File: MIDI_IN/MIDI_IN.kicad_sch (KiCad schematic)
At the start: 25 parts

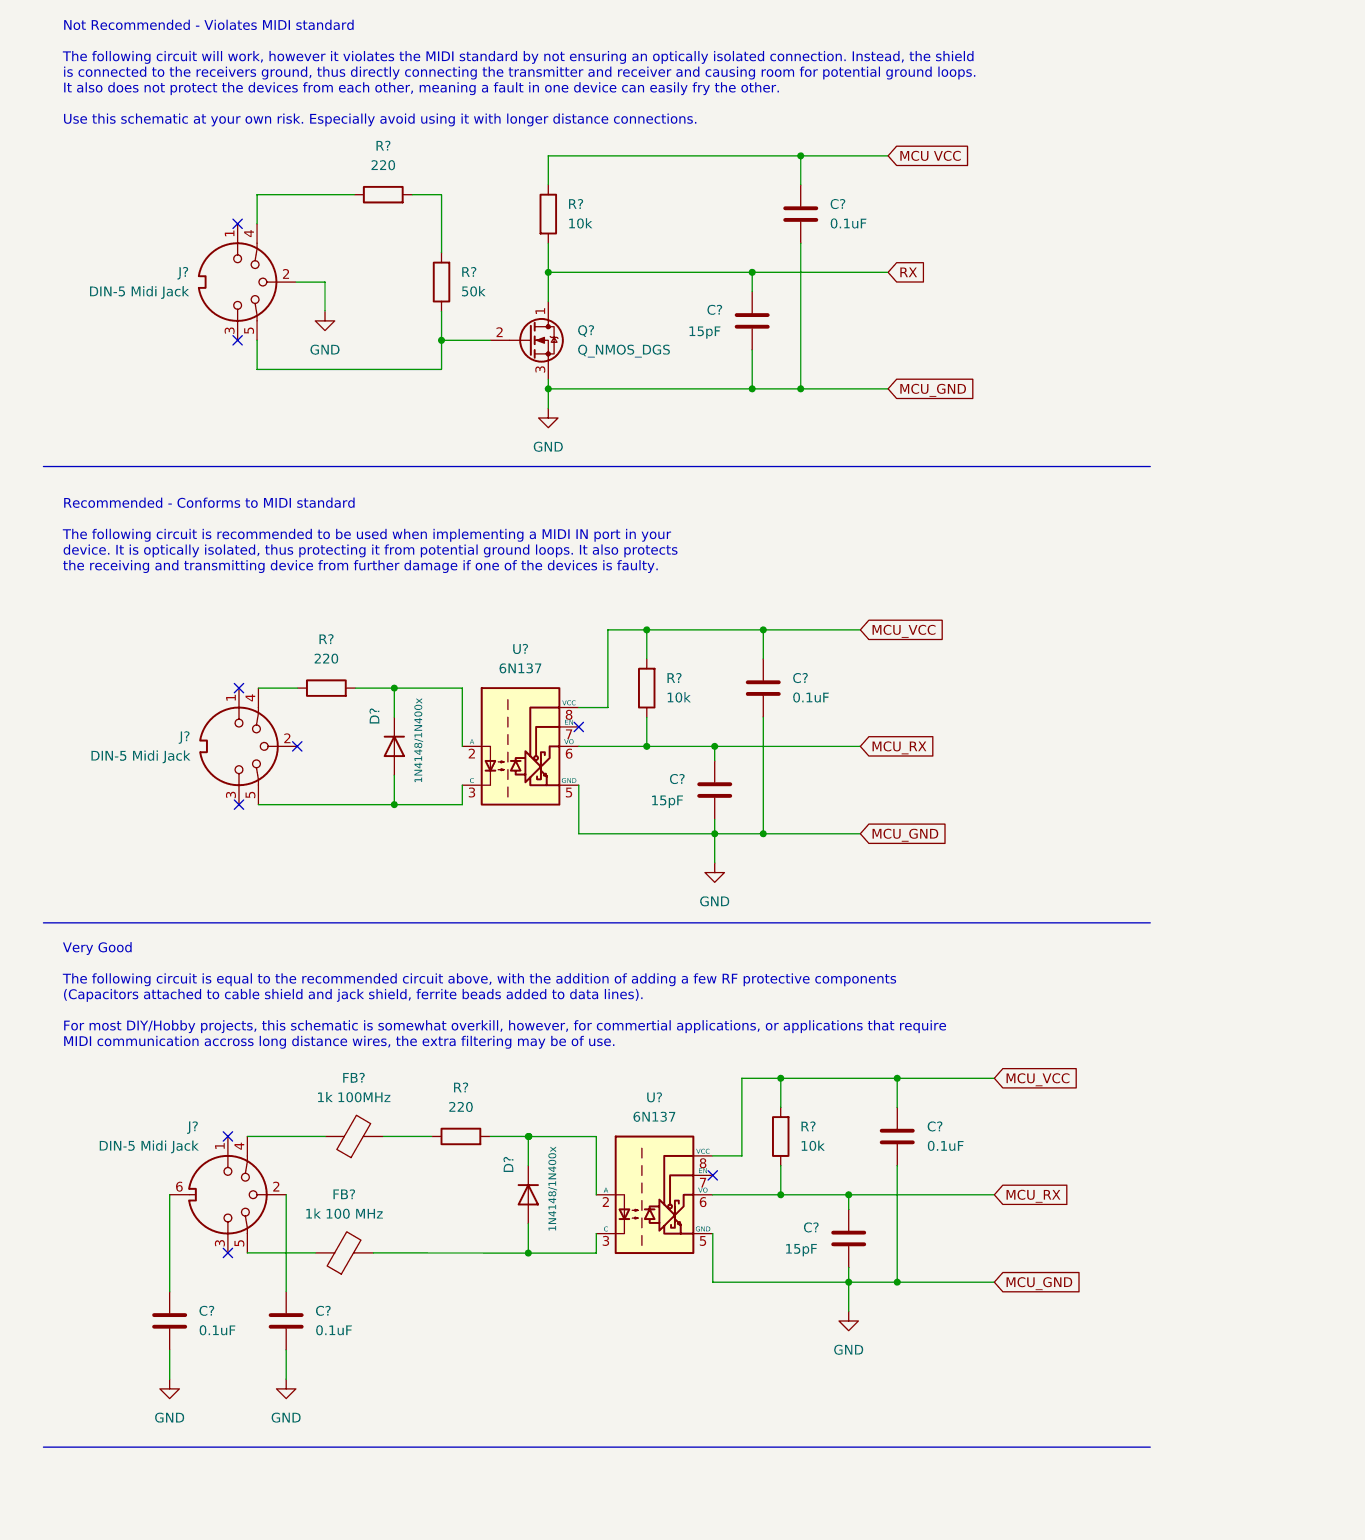
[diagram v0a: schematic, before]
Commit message: MIDI IN: Fixed optocoupler-less circuit + Fixed typo
Signed-off-by: CTXz <ctx.xda@gmail.com>
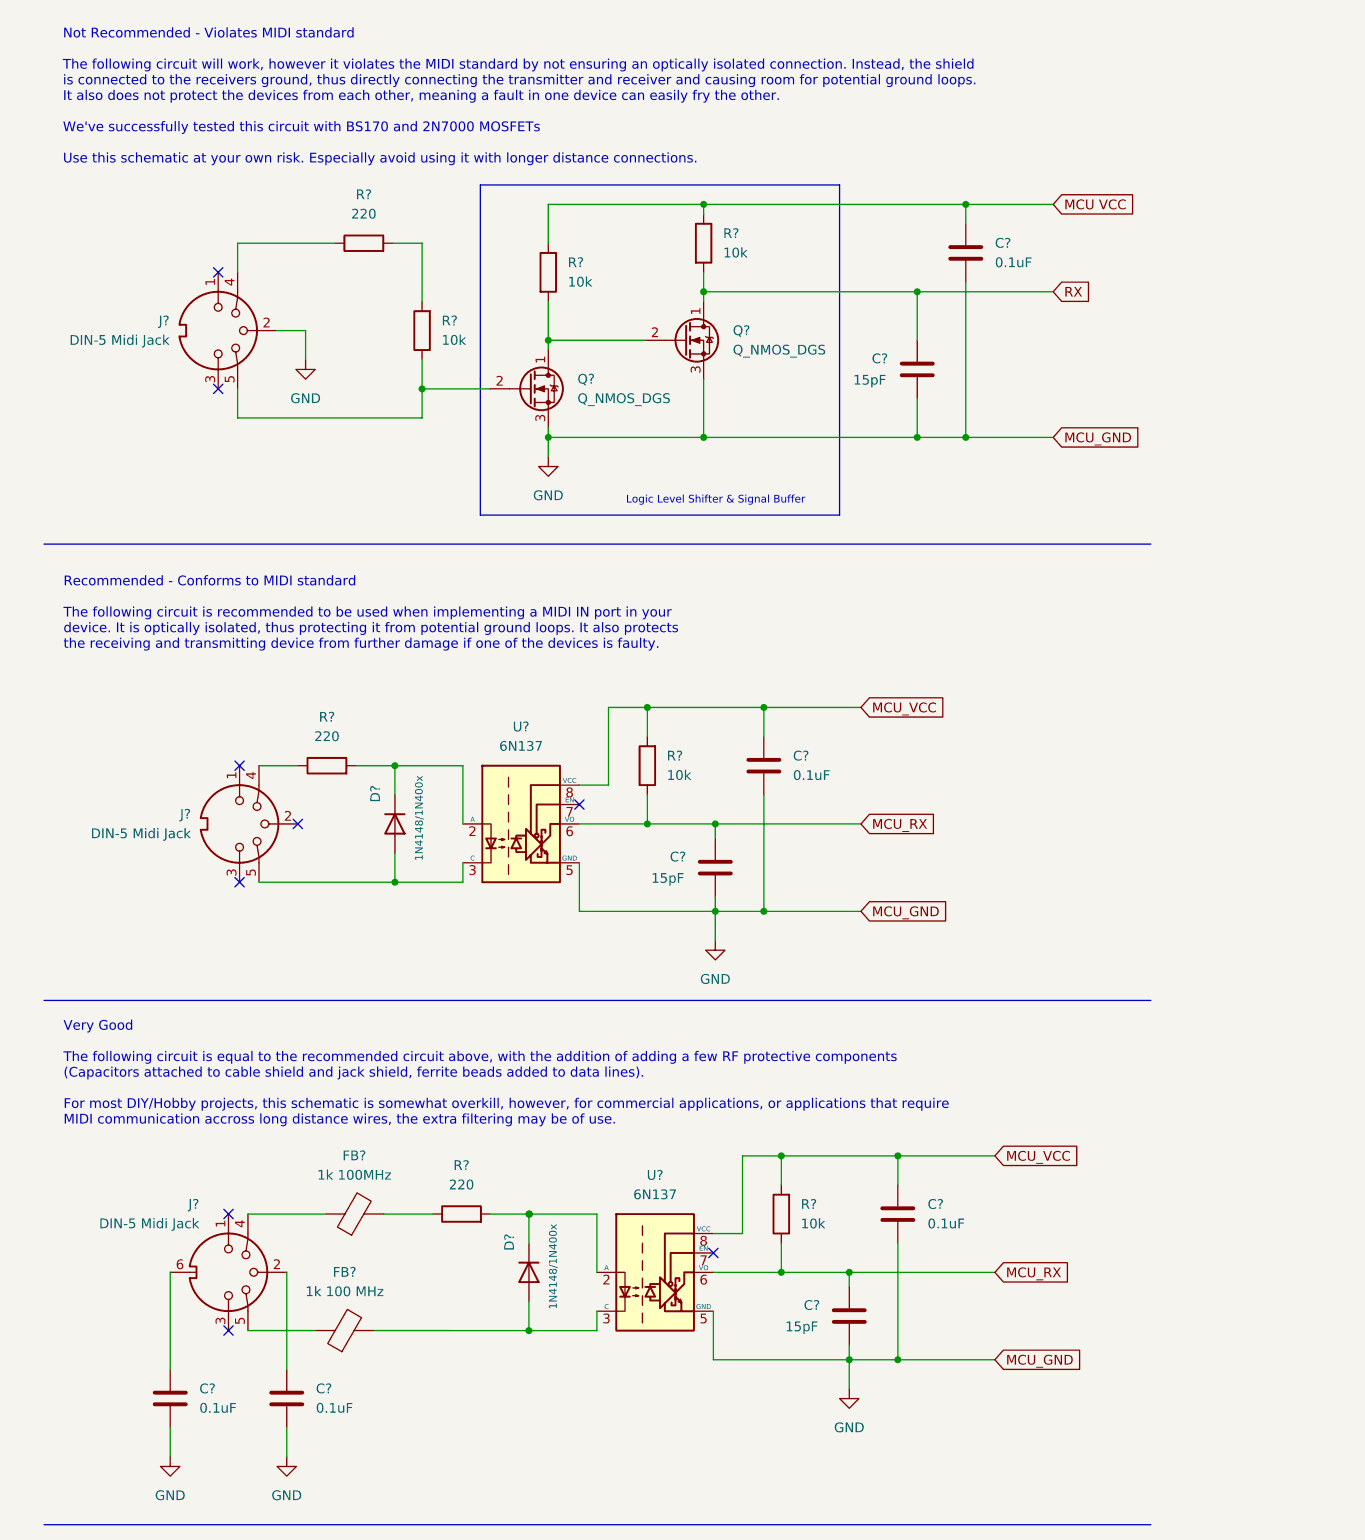
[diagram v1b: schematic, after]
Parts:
- added Q?: Q_NMOS_DGS, symbol Device:Q_NMOS_DGS
- added R?: 10k, symbol Device:R
- R?: value 50k -> 10k
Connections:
- net GND: now also Q?.3 (S)
- net MCU VCC: now also R?.1
- net RX: now also Q?.1 (D), R?.2; no longer Q?.1 (D), R?.2
- new net: Q?.1 (D), Q?.2 (G), R?.2
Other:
- note added: "Logic Level Shifter & Signal Buffer"
- note added: "Very Good The following circuit is equal to the recommended circuit above, with the addition of adding a few RF protective components (Capacitors attached to cable shield and jack shield, ferrite beads added to data lines). For most DIY/Hobby projects, this schematic is somewhat overkill, however, for commercial applications, or applications that require MIDI communication accross long distance w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"
- note removed: "Very Good The following circuit is equal to the recommended circuit above, with the addition of adding a few RF protective components (Capacitors attached to cable shield and jack shield, ferrite beads added to data lines). For most DIY/Hobby projects, this schematic is somewhat overkill, however, for commertial applications, or applications that require MIDI communication accross long distance w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"
- moved on the sheet: C?, D?, FB?, J?, Q?, R?, U?

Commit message: MIDI_IN: Minor improvements to schematic
Signed-off-by: CTXz <ctx.xda@gmail.com>
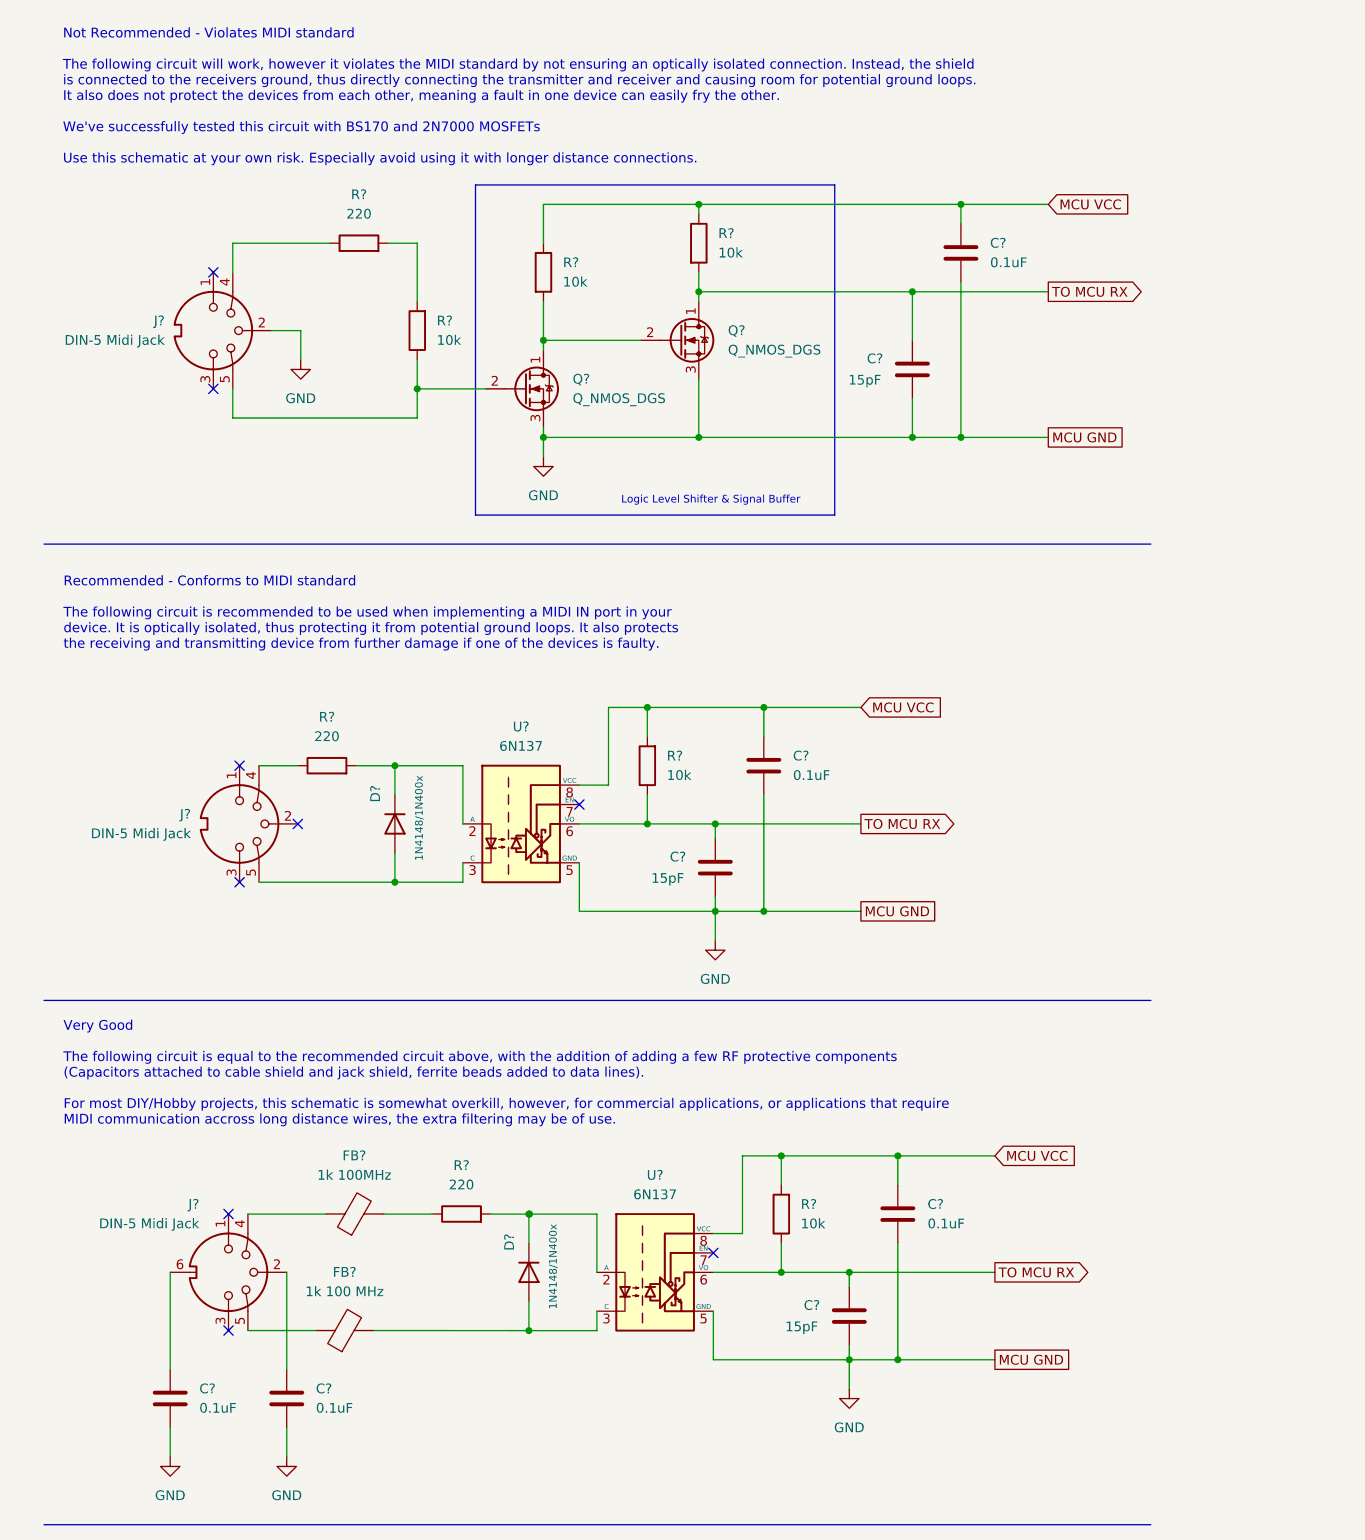
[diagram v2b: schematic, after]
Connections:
- net MCU_VCC is gone; now on net MCU VCC: C?.1, C?.1, R?.2, R?.2, U?.8 (VCC), U?.8 (VCC)
- net RX is gone; now on net TO MCU RX: C?.1, Q?.1 (D), R?.2
- net MCU_RX renamed TO MCU RX
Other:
- moved on the sheet: C?, J?, Q?, R?
